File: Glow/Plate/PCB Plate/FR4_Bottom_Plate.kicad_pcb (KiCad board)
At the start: 2 copper layers, 145.7 x 107.7 mm, 10 parts

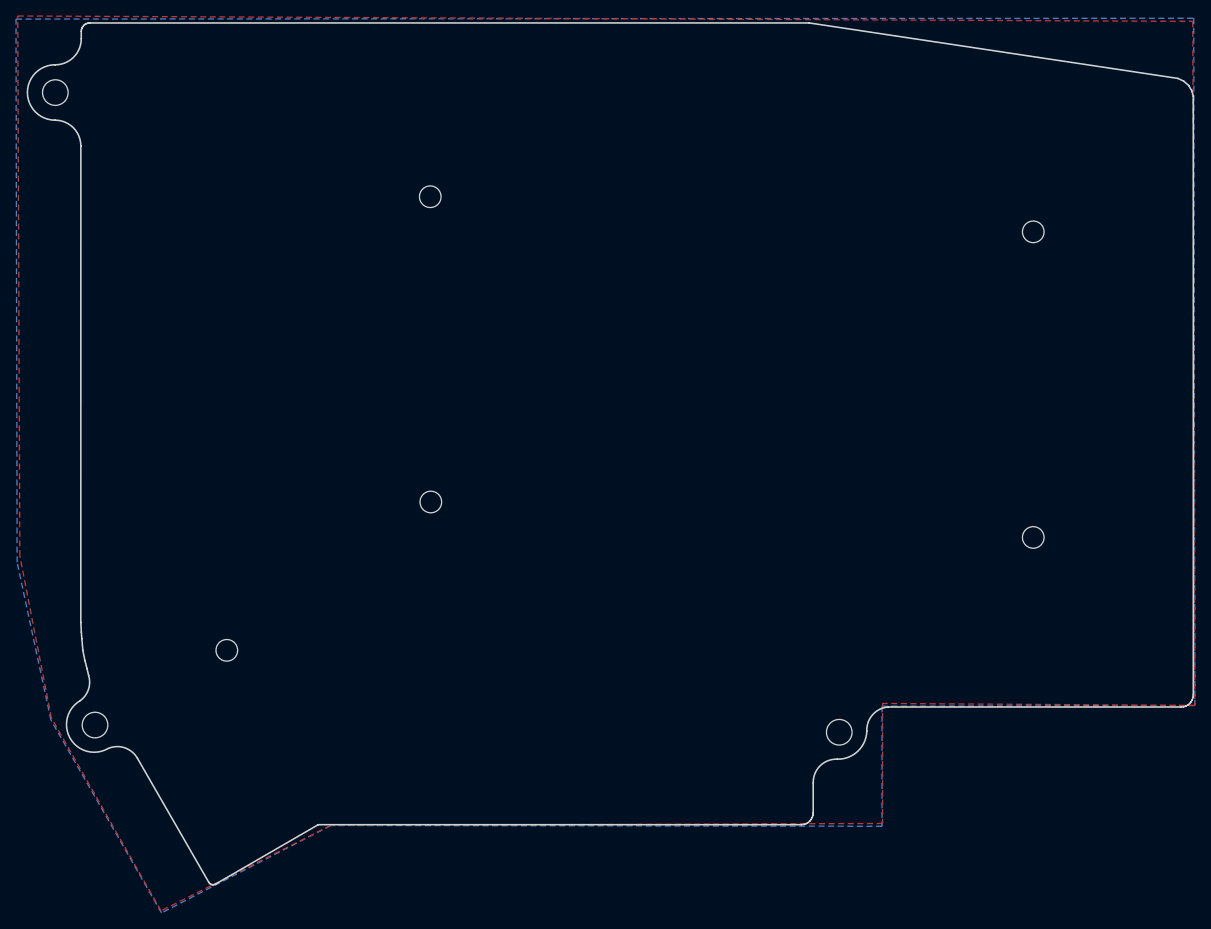
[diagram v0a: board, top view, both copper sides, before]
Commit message: Fixed Wrong No TENT bottom plate
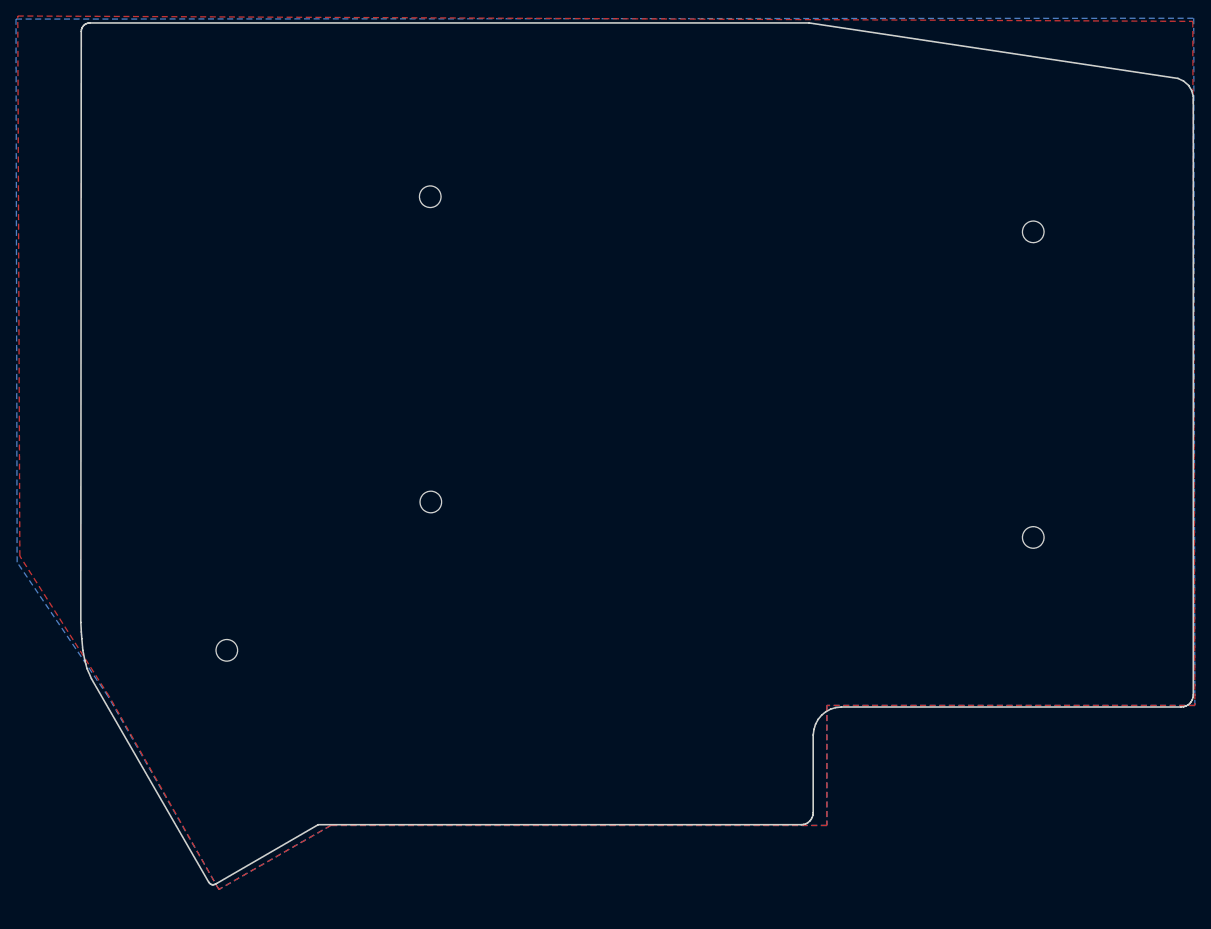
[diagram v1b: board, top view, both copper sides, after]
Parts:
- removed ? (x2): , 
- removed the TH7 at (77.5, 44.4)
- removed the TH7 at (175.4, 124.3)
- removed the TH7 at (82.4, 123.5)
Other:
- board size 145.7 x 107.7 mm -> 139.1 x 107.7 mm
